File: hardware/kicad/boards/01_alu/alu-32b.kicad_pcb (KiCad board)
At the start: 4 copper layers, 240 x 240 mm, 146 parts, among them J1 Conn_02x16_Odd_Even, J2 Conn_02x16_Odd_Even, J3 Conn_02x04_Odd_Even, J4 Conn_02x16_Odd_Even, J5 Conn_02x16_Counter_Clockwise, SW1 SW_DIP_x08, SW10 SW_DIP_x08, SW11 SW_DIP_x08, SW12 SW_DIP_x08, SW13 SW_DIP_x08, SW2 SW_DIP_x08, SW3 SW_DIP_x08, SW4 SW_DIP_x08, SW5 SW_DIP_x08, SW6 SW_DIP_x08, SW7 SW_SPDT, SW8 SW_DIP_x08, SW9 SW_DIP_x08, U1 74ACT151, U10 74ACT151, U11 74ACT151, U12 74ACT151, U13 74ACT151, U14 74ACT151, U15 74ACT151, U16 74ACT151, U17 74HC86, U18 74ACT151, U19 74HC00, U2 74ACT151, U20 74ACT283, U21 74ACT151, U22 74ACT151, U23 74ACT151, U24 74ACT151, U25 74ACT151, U26 74ACT151, U27 74HC86, U28 74ACT151, U29 74HC00, U3 74ACT151, U30 74ACT283, U31 74ACT151, U32 74ACT151, U33 74ACT151, U34 74ACT151, U35 74ACT151, U36 74ACT151, U37 74HC86, U38 74ACT151, U39 74HC00, U4 74ACT151, U40 74ACT283, U41 74ACT151, U47 74HC86, U49 74HC00, U5 74ACT151, U50 74ACT283, U57 74HC86, U59 74HC00, U6 74ACT151, U60 74ACT283, U67 74HC86, U69 74HC00, U7 74ACT151, U70 74ACT283, U77 74HC86, U79 74HC00, U8 74ACT151, U80 74ACT283, U87 74HC86, U89 74HC00, U9 74ACT151, U90 74ACT283

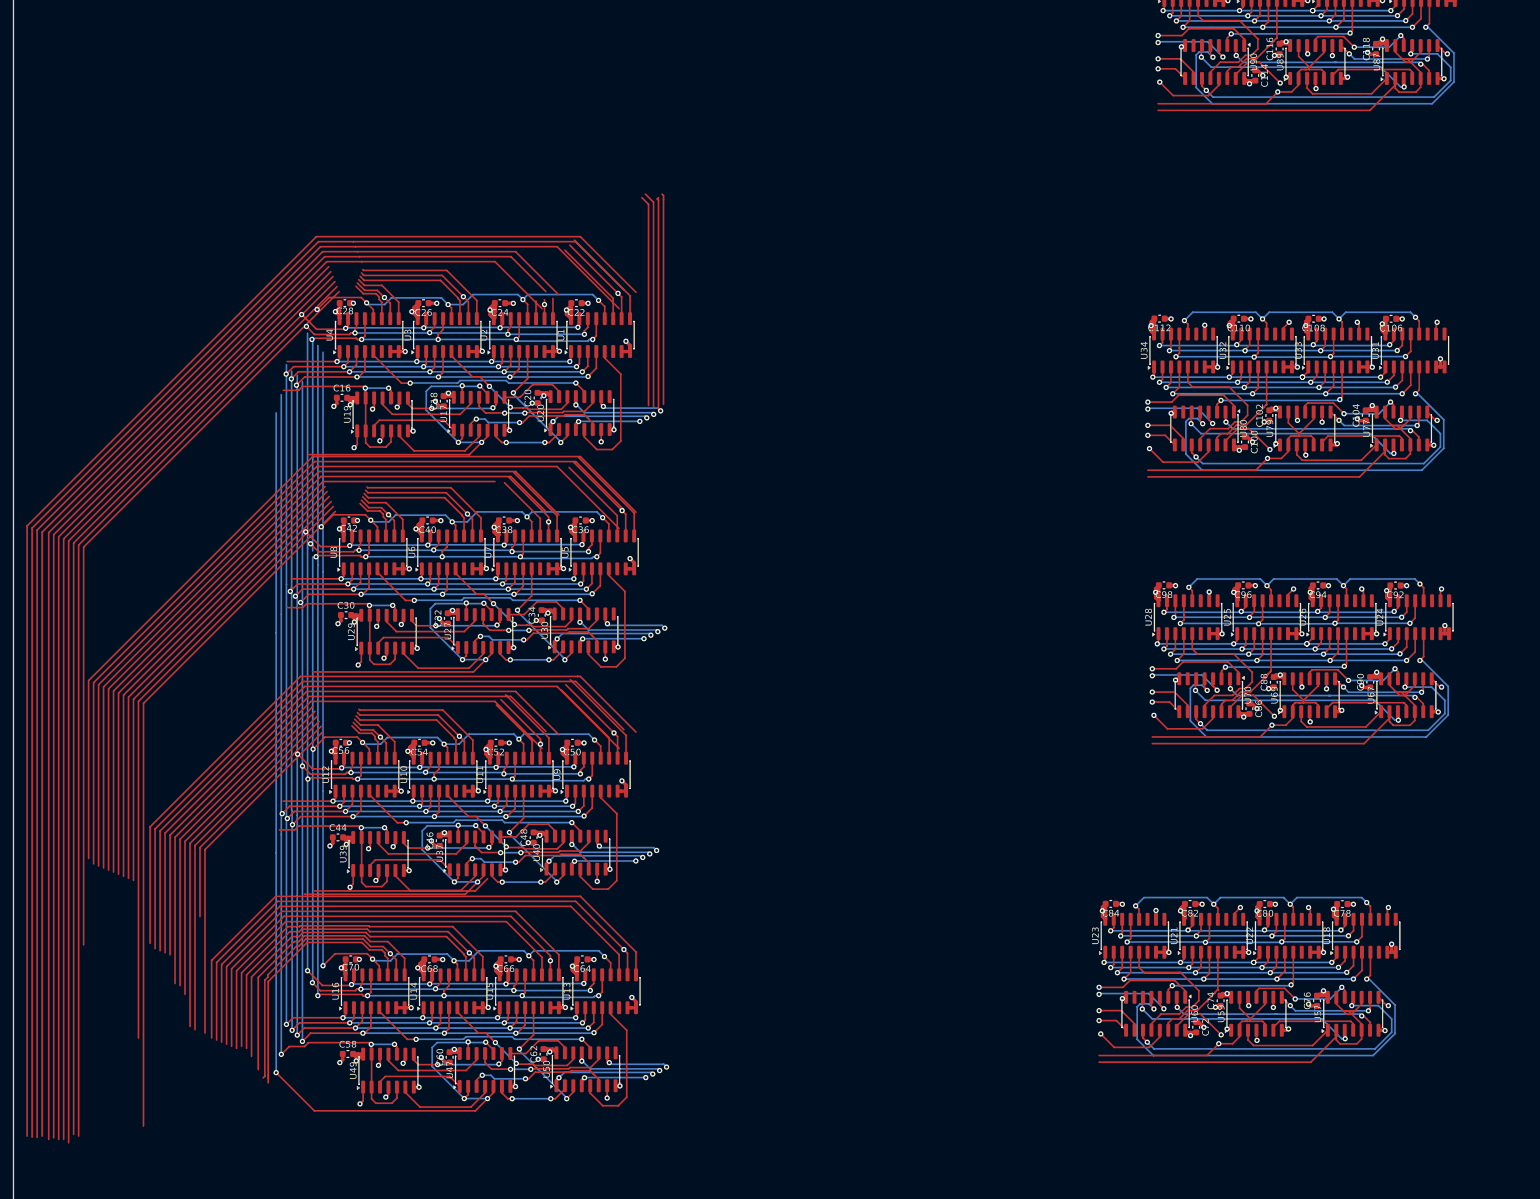
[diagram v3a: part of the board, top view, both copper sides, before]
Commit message: feat: routed right hand side cells; aligned bus traces; fixed DRC to 0 on each cell
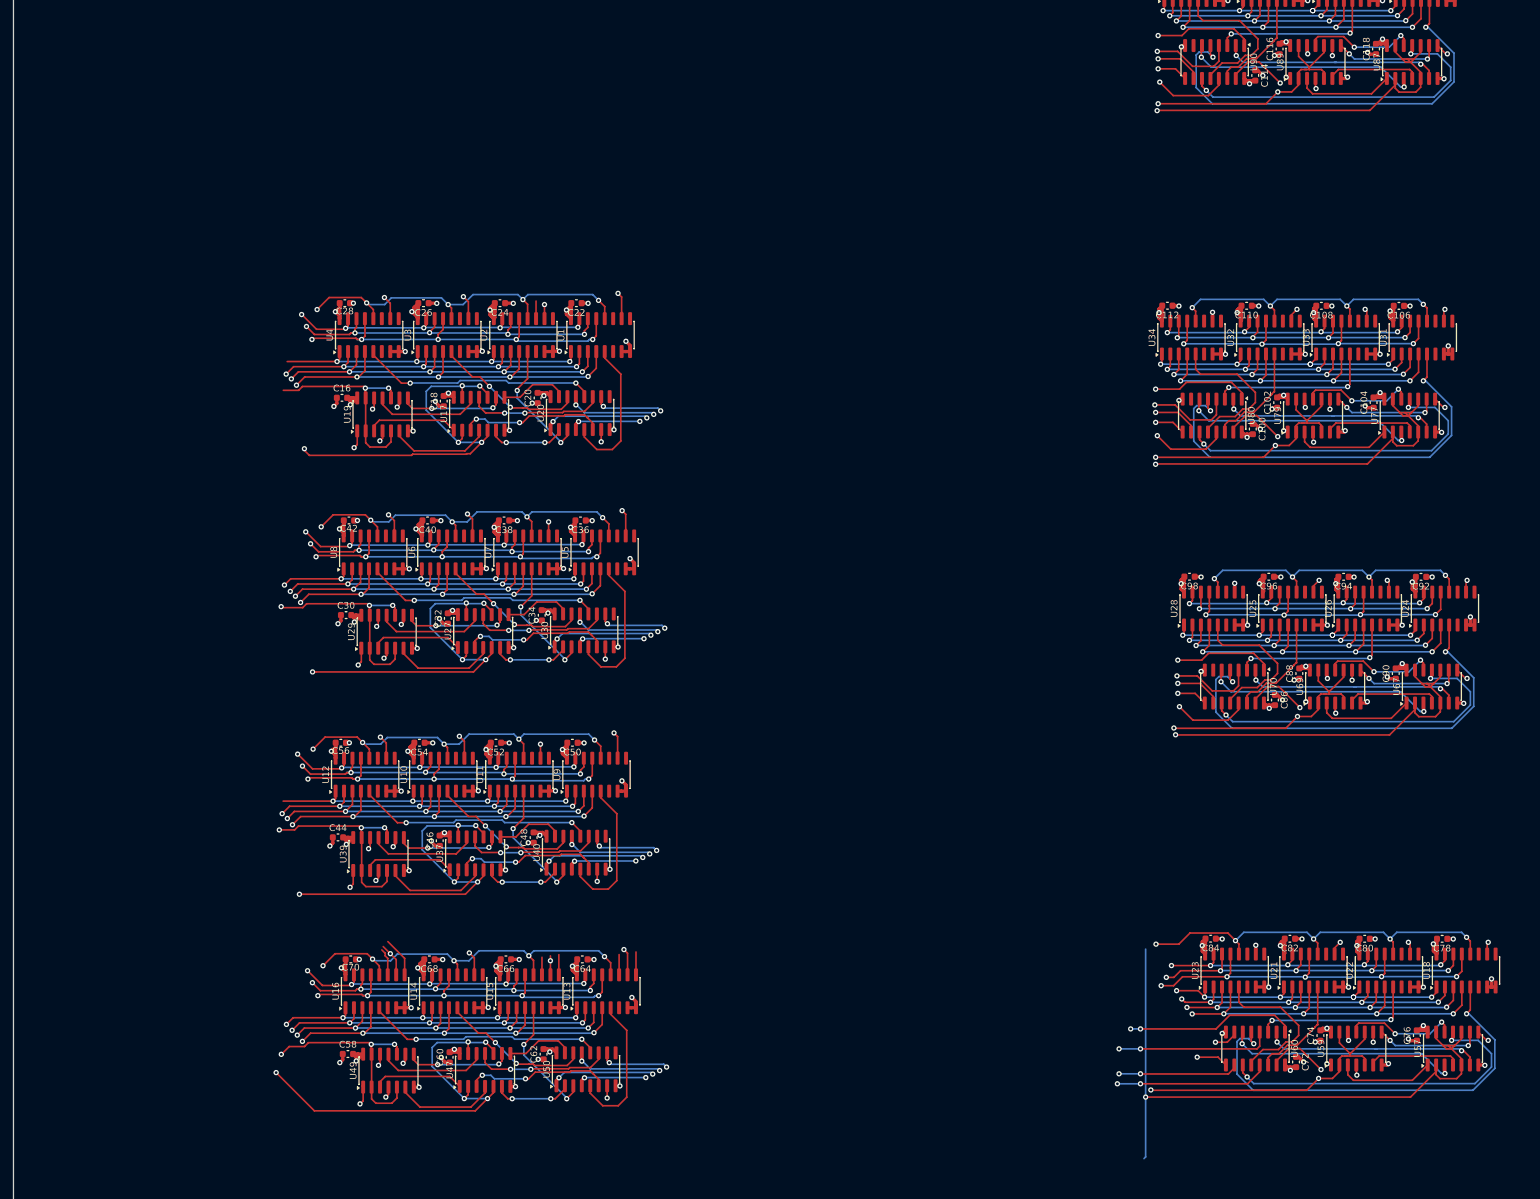
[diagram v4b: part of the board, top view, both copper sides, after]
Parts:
- moved U57 15.9 mm to (282.0, 290.4)
- moved C72 15.9 mm to (258.4, 292.5)
- moved U23 15.9 mm to (249.1, 278.7)
- moved U59 15.9 mm to (267.4, 290.4)
- moved U60 15.9 mm to (252.3, 290.4)
- moved C74 15.9 mm to (262.0, 288.5)
- moved C76 15.9 mm to (276.5, 288.5)
- moved C78 15.9 mm to (280.3, 274.0)
- moved C80 15.9 mm to (268.7, 273.9)
- moved C82 15.9 mm to (257.4, 273.9)
- moved C84 15.9 mm to (245.5, 273.9)
- moved U18 15.9 mm to (283.9, 278.7)
- moved U21 15.9 mm to (261.0, 278.7)
- moved U22 15.9 mm to (272.3, 278.7)
- moved U24 4.05 mm to (280.8, 224.3)
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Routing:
- net C0: track 421.5 -> 0.00 mm
- net C1: track 377.1 -> 0.00 mm
- net C8: track 219.4 -> 0.00 mm
- net A0: track 213.7 -> 0.00 mm
- net C9: track 186.3 -> 0.00 mm
- net A1: track 186.7 -> 2.64 mm
- net C2: track 169.9 -> 0.00 mm
- net A2: track 166.0 -> 0.00 mm
- net B2: track 195.0 -> 31.1 mm
- net C3: track 154.4 -> 0.00 mm
- net B3: track 173.3 -> 24.5 mm
- net C4: track 141.7 -> 0.00 mm
- net A4: track 136.3 -> 0.00 mm
- net B4: track 212.2 -> 78.1 mm
- net C5: track 124.1 -> 0.00 mm
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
